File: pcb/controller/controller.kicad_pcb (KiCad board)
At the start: 2 copper layers, 94 x 60.2 mm, 72 parts, among them J0 JST-HX_01x03, J1 Conn_01x24, J2 Conn_01x24, J3 Conn_01x05, J4 Conn_01x01, J5 Barrel_Jack, SW1 Button, SW2 Button, SW4 Button, U1 Teensy4.1

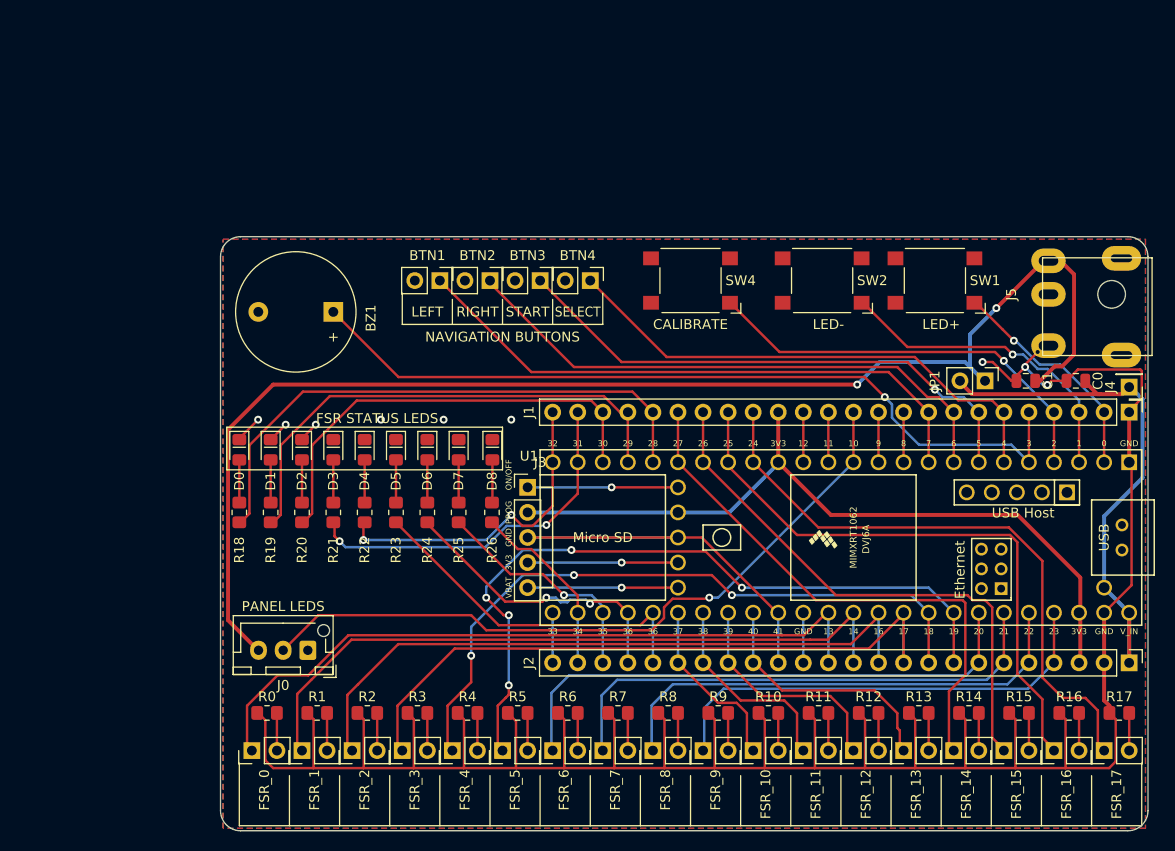
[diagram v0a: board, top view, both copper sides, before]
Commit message: Finalize v0.1 of breakout board to start v0.2
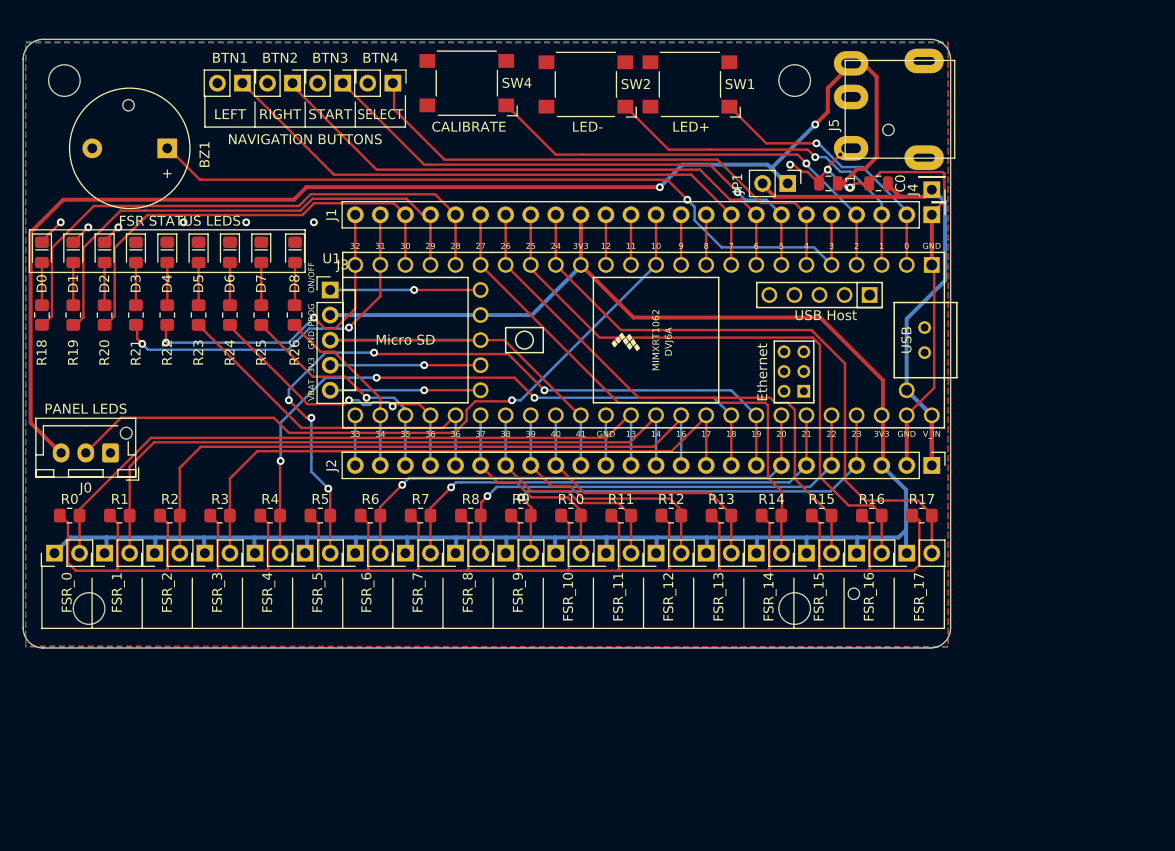
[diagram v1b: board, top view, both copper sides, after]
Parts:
- added H1: MountingHole, MountingHole:MountingHole_3.2mm_M3, F.Cu at (4.50, 4.50)
- added H2: MountingHole, MountingHole:MountingHole_3.2mm_M3, F.Cu at (78.5, 4.50)
- added H3: MountingHole, MountingHole:MountingHole_3.2mm_M3, F.Cu at (7.00, 58.0)
- added H4: MountingHole, MountingHole:MountingHole_3.2mm_M3, F.Cu at (78.5, 58.0)
- added H5: JCLPCB_Assy_Hole, widgetpad_parts:JCLPCB_Assembly_Hole, F.Cu at (11.0, 7.00)
- added H6: JCLPCB_Assy_Hole, widgetpad_parts:JCLPCB_Assembly_Hole, F.Cu at (88.0, 9.50)
- added H7: JCLPCB_Assy_Hole, widgetpad_parts:JCLPCB_Assembly_Hole, F.Cu at (84.5, 56.5)
- R0, R1, R10, R11, R12, R13, R14, R15, R16, R17, R2, R3, R4, R5, R6, R7, R8: value 10k -> 1k
- R9: value 220 -> 1k
- moved SW1 31.8 mm to (67.9, 4.89)
- moved SW2 31.1 mm to (57.3, 4.89)
- moved SW4 30.2 mm to (45.3, 4.76)
- moved FSR_8 28.3 mm to (44.1, 52.4)
- moved R11 28.3 mm to (60.9, 48.6)
- moved BTN1 28.3 mm to (22.5, 4.76)
- moved BTN2 28.3 mm to (27.6, 4.76)
- moved BTN3 28.3 mm to (32.7, 4.76)
- moved BTN4 28.3 mm to (37.8, 4.76)
- moved D7 28.3 mm to (24.4, 21.9)
- moved FSR_0 28.3 mm to (3.50, 52.4)
- moved FSR_1 28.3 mm to (8.57, 52.4)
- moved FSR_10 28.3 mm to (54.3, 52.4)
- moved FSR_11 28.3 mm to (59.4, 52.4)
- moved FSR_12 28.3 mm to (64.5, 52.4)
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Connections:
- FSR_0 pad 1: /FSR_0 -> +3V3
- FSR_0 pad 2: Net-(FSR_0-Pad2) -> /FSR_0
- FSR_1 pad 1: /FSR_1 -> +3V3
- FSR_1 pad 2: Net-(FSR_1-Pad2) -> /FSR_1
- FSR_10 pad 1: /FSR_10 -> +3V3
- FSR_10 pad 2: Net-(FSR_10-Pad2) -> /FSR_10
- FSR_11 pad 1: /FSR_11 -> +3V3
- FSR_11 pad 2: Net-(FSR_11-Pad2) -> /FSR_11
- FSR_12 pad 1: /FSR_12 -> +3V3
- FSR_12 pad 2: Net-(FSR_12-Pad2) -> /FSR_12
- FSR_13 pad 1: /FSR_13 -> +3V3
- FSR_13 pad 2: Net-(FSR_13-Pad2) -> /FSR_13
- FSR_14 pad 1: /FSR_14 -> +3V3
- FSR_14 pad 2: Net-(FSR_14-Pad2) -> /FSR_14
- FSR_15 pad 1: /FSR_15 -> +3V3
- FSR_15 pad 2: Net-(FSR_15-Pad2) -> /FSR_15
- FSR_16 pad 1: /FSR_16 -> +3V3
- FSR_16 pad 2: Net-(FSR_16-Pad2) -> /FSR_16
- FSR_17 pad 1: /FSR_17 -> +3V3
- FSR_17 pad 2: Net-(FSR_17-Pad2) -> /FSR_17
- FSR_2 pad 1: /FSR_2 -> +3V3
- FSR_2 pad 2: Net-(FSR_2-Pad2) -> /FSR_2
- FSR_3 pad 1: /FSR_3 -> +3V3
- FSR_3 pad 2: Net-(FSR_3-Pad2) -> /FSR_3
- FSR_4 pad 1: /FSR_4 -> +3V3
- FSR_4 pad 2: Net-(FSR_4-Pad2) -> /FSR_4
- FSR_5 pad 1: /FSR_5 -> +3V3
- FSR_5 pad 2: Net-(FSR_5-Pad2) -> /FSR_5
- FSR_6 pad 1: /FSR_6 -> +3V3
- FSR_6 pad 2: Net-(FSR_6-Pad2) -> /FSR_6
- FSR_7 pad 1: /FSR_7 -> +3V3
- FSR_7 pad 2: Net-(FSR_7-Pad2) -> /FSR_7
- FSR_8 pad 1: /FSR_8 -> +3V3
- FSR_8 pad 2: Net-(FSR_8-Pad2) -> /FSR_8
- FSR_9 pad 1: /FSR_9 -> +3V3
- FSR_9 pad 2: Net-(FSR_9-Pad2) -> /FSR_9
- R0 pad 2: Net-(FSR_0-Pad2) -> /FSR_0
- R1 pad 2: Net-(FSR_1-Pad2) -> /FSR_1
- R10 pad 2: Net-(FSR_10-Pad2) -> /FSR_10
- R11 pad 2: Net-(FSR_11-Pad2) -> /FSR_11
- R12 pad 2: Net-(FSR_12-Pad2) -> /FSR_12
- R13 pad 2: Net-(FSR_13-Pad2) -> /FSR_13
- R14 pad 2: Net-(FSR_14-Pad2) -> /FSR_14
- R15 pad 2: Net-(FSR_15-Pad2) -> /FSR_15
- R16 pad 2: Net-(FSR_16-Pad2) -> /FSR_16
- R17 pad 2: Net-(FSR_17-Pad2) -> /FSR_17
- R2 pad 2: Net-(FSR_2-Pad2) -> /FSR_2
- R3 pad 2: Net-(FSR_3-Pad2) -> /FSR_3
- R4 pad 2: Net-(FSR_4-Pad2) -> /FSR_4
- R5 pad 2: Net-(FSR_5-Pad2) -> /FSR_5
- R6 pad 2: Net-(FSR_6-Pad2) -> /FSR_6
- R7 pad 2: Net-(FSR_7-Pad2) -> /FSR_7
- R8 pad 2: Net-(FSR_8-Pad2) -> /FSR_8
- R9 pad 2: Net-(FSR_9-Pad2) -> /FSR_9
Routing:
- net +3V3: track 77.3 -> 198.1 mm
- net /SPEAKER: track 82.7 -> 77.8 mm
- net /BTN_BRGHT_UP: track 22.8 -> 27.5 mm
- net /BTN_BRGHT_DOWN: track 32.4 -> 36.2 mm
- net Net-(FSR_9-Pad2): track 3.81 -> 0.00 mm
- net Net-(FSR_8-Pad2): track 3.81 -> 0.00 mm
- net Net-(FSR_7-Pad2): track 3.81 -> 0.00 mm
- net Net-(FSR_6-Pad2): track 3.81 -> 0.00 mm
- net Net-(FSR_5-Pad2): track 3.81 -> 0.00 mm
- net Net-(FSR_4-Pad2): track 3.81 -> 0.00 mm
- net Net-(FSR_3-Pad2): track 3.81 -> 0.00 mm
- net Net-(FSR_2-Pad2): track 3.81 -> 0.00 mm
- net Net-(FSR_17-Pad2): track 3.81 -> 0.00 mm
- net Net-(FSR_16-Pad2): track 3.81 -> 0.00 mm
- net Net-(FSR_15-Pad2): track 3.81 -> 0.00 mm
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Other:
- board size 94 x 60.2 mm -> 94 x 61.7 mm
- board text added: "JLCJLCJLCJLC"

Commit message: Schematic and layout of v0.2
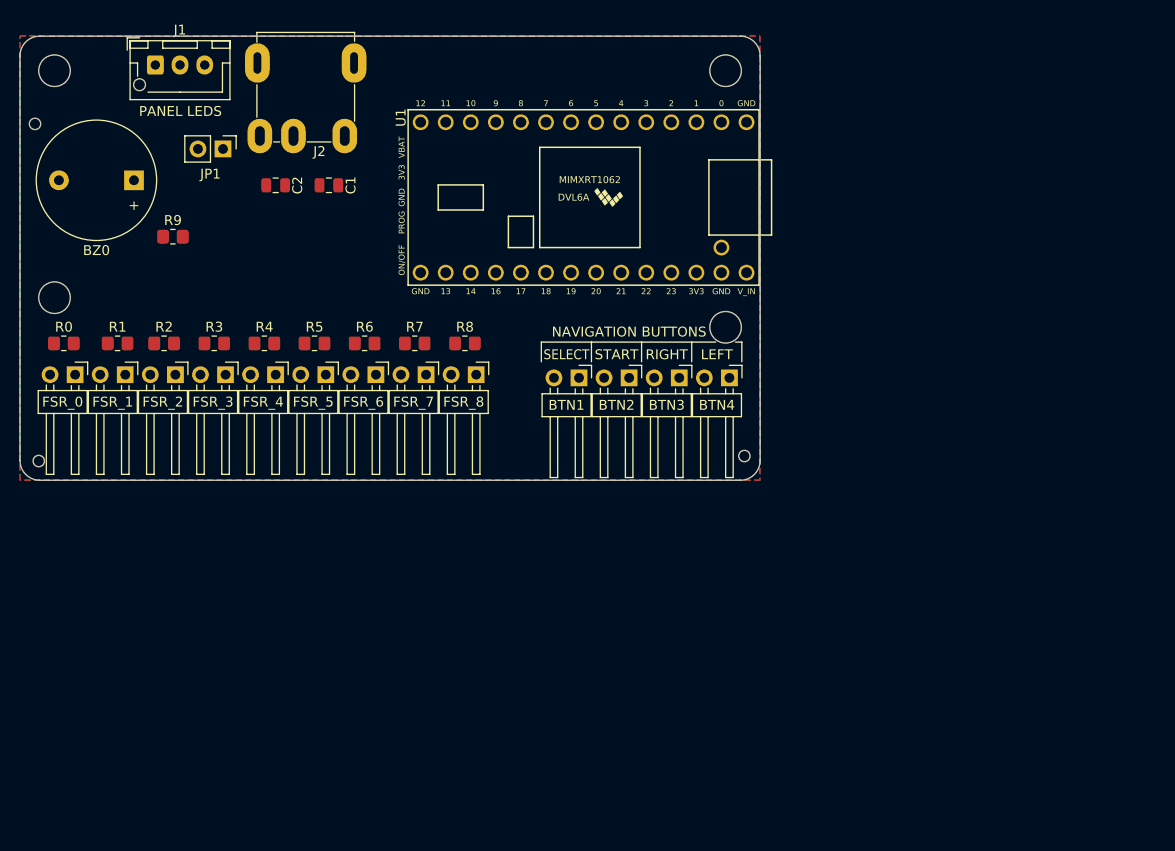
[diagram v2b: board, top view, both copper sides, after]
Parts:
- removed D0, D1, D2, D3, D4, D5, D6, D7, D8: LED, LED_SMD:LED_0805_2012Metric_Pad1.15x1.40mm_HandSolder
- removed FSR_10, FSR_11, FSR_12, FSR_13, FSR_14, FSR_15, FSR_16, FSR_17, FSR_9: FSR, Connector_PinHeader_2.54mm:PinHeader_1x02_P2.54mm_Vertical
- removed the J1 at (92.4, 18.1)
- removed the J2 at (92.4, 43.5)
- removed J3: Conn_01x05, Connector_PinHeader_2.54mm:PinHeader_1x05_P2.54mm_Vertical
- removed J4: Conn_01x01, Connector_PinHeader_2.54mm:PinHeader_1x01_P2.54mm_Vertical
- removed R10, R11, R12, R13, R14, R15, R16, R17: 1k, Resistor_SMD:R_0805_2012Metric_Pad1.20x1.40mm_HandSolder
- removed R18, R19, R20, R21, R22, R23, R24, R25, R26: 220, Resistor_SMD:R_0805_2012Metric_Pad1.20x1.40mm_HandSolder
- removed SW1, SW2, SW4: Button, Button_Switch_SMD:SW_SPST_Omron_B3FS-100xP
- BTN1, BTN2, BTN3, BTN4: footprint Connector_PinHeader_2.54mm:PinHeader_1x02_P2.54mm_Vertical -> widgetpad-parts:PinHeader_1x02_P2.54mm_Horizontal
- FSR_0, FSR_1, FSR_2, FSR_3, FSR_4, FSR_5, FSR_6, FSR_7, FSR_8: footprint Connector_PinHeader_2.54mm:PinHeader_1x02_P2.54mm_Vertical -> widgetpad_parts:PinHeader_1x02_P2.54mm_Horizontal
- R9: value 1k -> 220
- U1: value Teensy4.1 -> Teensy4.0; footprint teensy:Teensy41 -> widgetpad_parts:teensy40
- moved H6 92.4 mm to (1.91, 43.1)
- moved H1 84.4 mm to (71.5, 3.50)
- moved H5 81.3 mm to (3.50, 26.5)
- moved J2 63.0 mm to (27.7, 3.72), turned to 0 degrees
- moved JP1 57.3 mm to (20.6, 11.4)
- moved C2 56.0 mm to (25.9, 15.1)
- moved C1 55.7 mm to (31.3, 15.1)
- moved BTN3 45.3 mm to (66.8, 34.6)
- moved BTN4 45.3 mm to (71.9, 34.6)
- moved BTN1 45.3 mm to (56.6, 34.6)
- moved BTN2 45.3 mm to (61.7, 34.6)
- moved R9 45.2 mm to (15.5, 20.3)
- moved J1 39.6 mm to (13.7, 2.92), turned to 0 degrees
- moved U1 33.4 mm to (39.3, 7.45)
- moved H4 26.0 mm to (71.5, 29.5)
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- renumbered BZ1 to BZ0, C0 to C1, C1 to C2, H1 to H0, H3 to H1, H5 to H2, H7 to H3, H2 to H4, H4 to H5, J0 to J1, J5 to J2
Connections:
- BZ0 pad 1: /SPEAKER -> Net-(BZ0-Pad1)
- R9 pad 1: GND -> /SPEAKER
- R9 pad 2: /FSR_9 -> Net-(BZ0-Pad1)
- U1 pad 20: /FSR_LED_0 -> unconnected-(U1-Pad20)
- U1 pad 21: /FSR_LED_1 -> /FSR_0
- U1 pad 22: /FSR_LED_2 -> /FSR_1
- U1 pad 23: /FSR_LED_3 -> /FSR_2
- U1 pad 24: /FSR_LED_4 -> /FSR_3
- U1 pad 25: /FSR_LED_9 -> /FSR_4
- U1 pad 26: /FSR_LED_8 -> /FSR_5
- U1 pad 27: /FSR_LED_7 -> /FSR_6
- U1 pad 28: /FSR_LED_6 -> /FSR_7
- U1 pad 29: /FSR_LED_5 -> /FSR_8
- U1 pad 30: /FSR_10 -> unconnected-(U1-Pad30)
- U1 pad 31: /FSR_11 -> unconnected-(U1-Pad31)
- U1 pad 32: /FSR_12 -> GND
- U1 pad 33: /FSR_13 -> +5V
- U1 pad 34: GND -> +5V
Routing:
- net GND: track 301.3 -> 0.00 mm, vias 10 -> 0
- net +3V3: track 198.1 -> 0.00 mm
- net VDC: track 135.5 -> 0.00 mm, vias 2 -> 0
- net /SPEAKER: track 77.8 -> 0.00 mm, vias 1 -> 0
- net /FSR_5: track 75.1 -> 0.00 mm, vias 5 -> 0
- net /LED_OUT: track 72.5 -> 0.00 mm, vias 1 -> 0
- net /FSR_1: track 69.3 -> 0.00 mm
- net /FSR_0: track 69.1 -> 0.00 mm
- net /FSR_3: track 68.2 -> 0.00 mm
- net /FSR_4: track 67.3 -> 0.00 mm, vias 3 -> 0
- net /FSR_2: track 66.4 -> 0.00 mm
- net /FSR_17: track 64.3 -> 0.00 mm
- net /FSR_16: track 62.9 -> 0.00 mm
- net /BTN_ARROW_LEFT: track 59.9 -> 0.00 mm
- net /BTN_ARROW_RIGHT: track 57.3 -> 0.00 mm
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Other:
- board size 94 x 61.7 mm -> 75 x 45 mm
- net class Default removed
- net class Power removed
- board text removed: "0"
- board text removed: "1"
- board text removed: "10"
- board text removed: "11"
- board text removed: "12"
- board text removed: "13"
- board text removed: "14"
- board text removed: "16"
- board text removed: "17"
- board text removed: "18"
- board text removed: "19"
- board text removed: "2"
- board text removed: "20"
- board text removed: "21"
- board text removed: "22"
- board text removed: "23"
- board text removed: "24"
- board text removed: "25"
- board text removed: "26"
- board text removed: "27"
- board text removed: "28"
- board text removed: "29"
- board text removed: "3"
- board text removed: "30"
- board text removed: "31"
- board text removed: "32"
- board text removed: "33"
- board text removed: "34"
- board text removed: "35"
- board text removed: "36"
- board text removed: "37"
- board text removed: "38"
- board text removed: "39"
- board text removed: "3V3"
- board text removed: "4"
- board text removed: "40"
- board text removed: "41"
- board text removed: "5"
- board text removed: "6"
- board text removed: "7"
- board text removed: "8"
- board text removed: "9"
- board text removed: "CALIBRATE"
- board text removed: "FSR STATUS LEDS"
- board text removed: "GND"
- board text removed: "LED+"
- board text removed: "LED-"
- board text removed: "ON/OFF"
- board text removed: "PROG"
- board text removed: "VBAT"
- board text removed: "V_IN"

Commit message: Widgetpad controller v0.2
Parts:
- moved R1 0.37 mm to (9.53, 31.1)
- turned R9 to 180 degrees
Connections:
- U1 pad 31: unconnected-(U1-Pad31) -> +3V3
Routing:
- net +5V: track 0.00 -> 152.8 mm
- net +3V3: track 0.00 -> 83.0 mm
- net /SPEAKER: track 0.00 -> 54.4 mm
- net /FSR_0: track 0.00 -> 45.4 mm
- net /FSR_1: track 0.00 -> 42.7 mm
- net /FSR_2: track 0.00 -> 40.4 mm
- net /FSR_3: track 0.00 -> 37.9 mm
- net /LED_OUT: track 0.00 -> 35.9 mm
- net /FSR_4: track 0.00 -> 35.3 mm
- net /BTN_SELECT: track 0.00 -> 34.2 mm
- net /BTN_ARROW_LEFT: track 0.00 -> 33.8 mm
- net /BTN_ARROW_RIGHT: track 0.00 -> 33.0 mm
- net /FSR_5: track 0.00 -> 32.7 mm
- net /BTN_START: track 0.00 -> 31.8 mm
- net /FSR_6: track 0.00 -> 30.2 mm
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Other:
- board text added: "Widgetpad Controller Breakout v0 github.com/widget-/widgetpad ©Widget 2022, Licensed GPLv2"
- board text removed: "Widgetpad Controller Breakout v0 github.com/widget-/widgetpad ©Widget 2021, Licensed GPLv2"
